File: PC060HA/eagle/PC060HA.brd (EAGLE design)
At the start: 36.7 x 39.6 mm, 13 parts, among them IC22 PC060HA, IC8 LM1117MPX-3.3

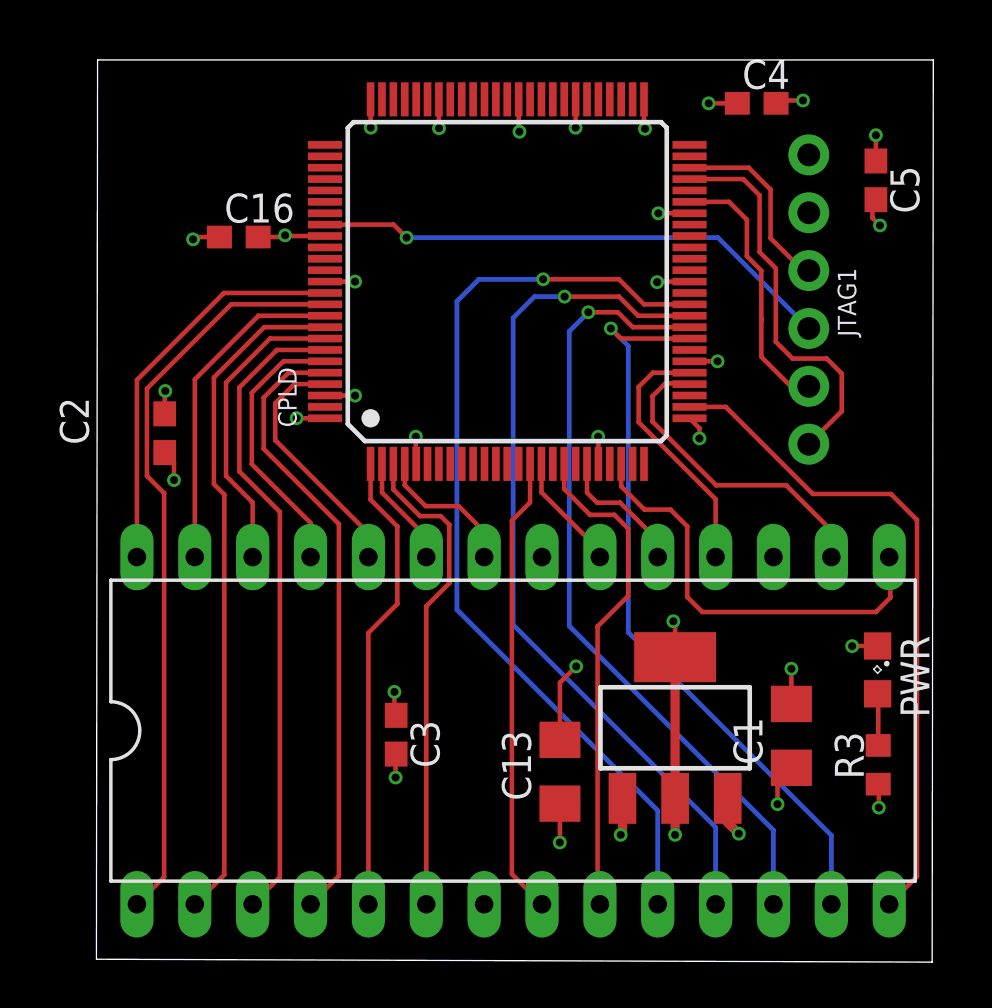
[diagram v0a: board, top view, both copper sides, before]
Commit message: shrunk down to small board with SMD DiL
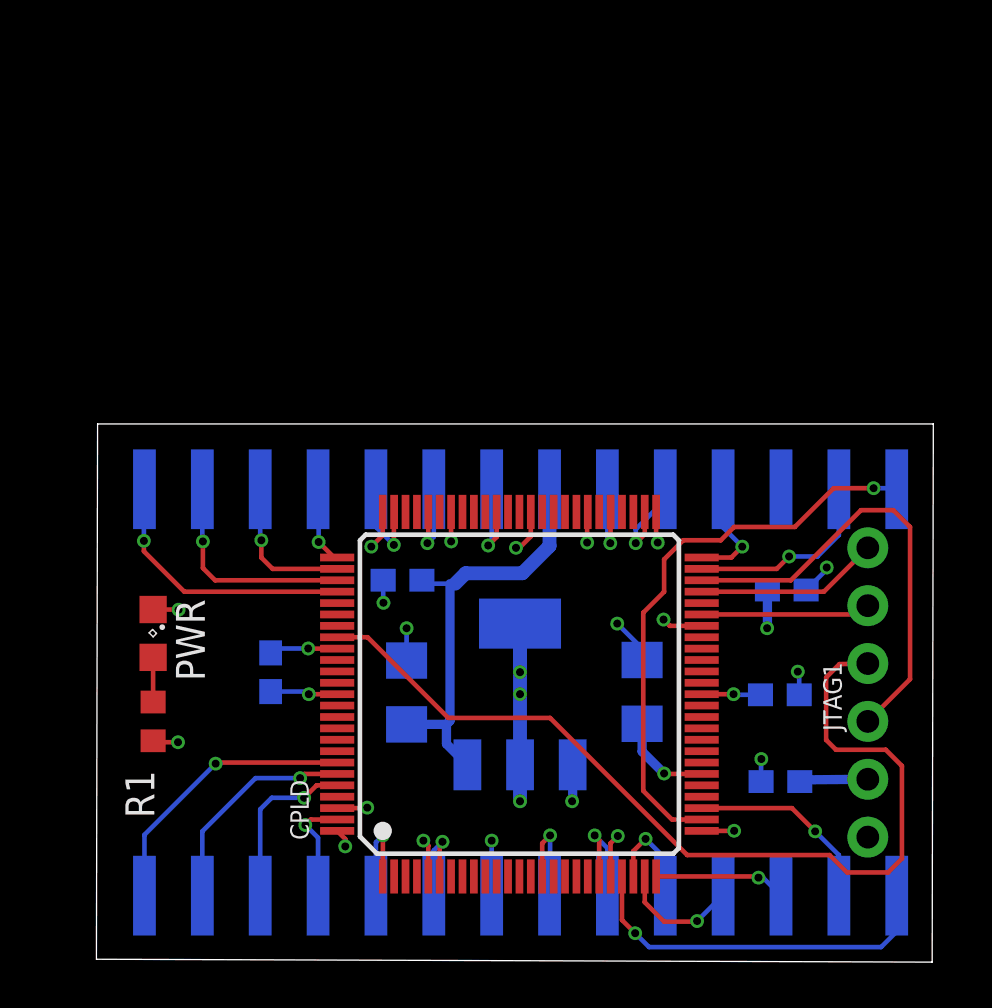
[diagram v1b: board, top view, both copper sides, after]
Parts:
- removed C13: 1uF, rcl:C1206
- removed C16: 1uF, eagle-ltspice:C0603
- removed IC22: PC060HA, OpWolf:DIL28-6
- removed R3: 10k, rcl:R0603
- added C6: 1uF, eagle-ltspice:C0603
- added C7: 1uF, rcl:C1206
- added J1: (no value), SamacSys_Parts:1501062800106161
- added R1: 10k, rcl:R0603
- C1: value 100nF -> 10uF
- C3: value 10uF -> 10nF
- moved PWR 31.8 mm to (2.49, 14.3)
- moved C4 29.8 mm to (30.0, 7.80), flipped to the bottom, turned to 180 degrees
- moved C5 23.0 mm to (30.0, 11.6), flipped to the bottom, turned to 180 degrees
- moved CPLD 18.1 mm to (18.6, 11.6)
- moved JTAG1 17.4 mm to (33.9, 11.7), turned to 270 degrees
- moved C1 17.0 mm to (13.6, 11.7), flipped to the bottom
- moved C2 11.5 mm to (7.65, 12.6), flipped to the bottom
- moved IC8 6.96 mm to (18.6, 11.6), flipped to the bottom
- moved C3 6.79 mm to (13.4, 16.6), flipped to the bottom, turned to 0 degrees
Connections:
- removed net !SNMI: CPLD.34, IC22.12
- new net !NMI: CPLD.25, J1.17
- net !IC: now also CPLD.52, J1.10; no longer CPLD.20, IC22.19
- net !MCS: now also CPLD.79, J1.1; no longer CPLD.89, IC22.28
- net !MRD: now also CPLD.77, J1.3; no longer CPLD.93, IC22.26
- net !MWR: now also CPLD.78, J1.2; no longer CPLD.91, IC22.27
- net !PG: now also CPLD.50, J1.11; no longer CPLD.30, IC22.18
- net !ROUT: now also CPLD.28, J1.16; no longer CPLD.33, IC22.13
- net !SCS: now also CPLD.94, J1.28; no longer CPLD.90, IC22.1
- net !SRD: now also CPLD.96, J1.26; no longer CPLD.94, IC22.3
- net !SWR: now also CPLD.95, J1.27; no longer CPLD.92, IC22.2
- net AMP: now also CPLD.49, J1.13; no longer CPLD.29, IC22.16
- net GND: now also C6.2, C7.2, J1.22; no longer C13.2, C16.2, IC22.7
- net IN0: now also CPLD.23, J1.19; no longer CPLD.36, IC22.10
- net IN1: now also CPLD.24, J1.18; no longer CPLD.35, IC22.11
- net MA0: now also CPLD.76, J1.4; no longer CPLD.95, IC22.25
- net MCLK: now also CPLD.27, J1.14; no longer CPLD.23, IC22.15
- net MD0: now also CPLD.74, J1.5; no longer CPLD.97, IC22.24
- net MD1: now also CPLD.71, J1.6; no longer CPLD.2, IC22.23
- net MD2: now also CPLD.65, J1.7; no longer CPLD.4, IC22.22
- net MD3: now also CPLD.55, J1.9; no longer CPLD.16, IC22.20
- net N$18: now also R1.2; no longer R3.2
- net SA0: now also CPLD.99, J1.25; no longer CPLD.96, IC22.4
- net SCLK: now also CPLD.22, J1.15; no longer CPLD.27, IC22.14
- net SD0: now also J1.24; no longer IC22.5
- net SD1: now also CPLD.6, J1.23; no longer CPLD.3, IC22.6
- net SD2: now also J1.21; no longer IC22.8
- net SD3: now also CPLD.20, J1.20; no longer CPLD.18, IC22.9
- net VCC: now also J1.8; no longer IC22.21
- net VCC33: now also C6.1, C7.1, R1.1; no longer C13.1, C16.1, R3.1
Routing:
- net IN0: track 41.2 -> 4.72 mm
- net !SNMI: track 34.8 -> 0.00 mm, vias 1 -> 0
- net IN1: track 37.9 -> 5.40 mm
- net !ROUT: track 32.9 -> 8.66 mm
- net SA0: track 27.3 -> 4.83 mm, vias 0 -> 1
- net !SRD: track 28.4 -> 7.61 mm, vias 0 -> 1
- net !SCS: track 32.8 -> 12.4 mm, vias 0 -> 1
- net !SWR: track 29.6 -> 9.79 mm, vias 0 -> 1
- net TDO: track 23.1 -> 42.0 mm, vias 1 -> 0
- net SD1: track 21.3 -> 4.10 mm, vias 0 -> 1
- net SD3: track 21.7 -> 4.76 mm, vias 0 -> 1
- net SD0: track 20.3 -> 4.58 mm, vias 0 -> 1
- net SD2: track 20.2 -> 4.60 mm, vias 0 -> 1
- net VCC: track 4.66 -> 19.0 mm, vias 3 -> 0
- net SCLK: track 29.4 -> 16.3 mm, vias 0 -> 1
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- removed copper zone on layer 15, net VCC
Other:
- board size 36.7 x 39.6 mm -> 36.7 x 23.6 mm
